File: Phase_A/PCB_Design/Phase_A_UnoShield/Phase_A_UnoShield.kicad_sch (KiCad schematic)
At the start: 23 parts, among them J1 Power, J2 Digital/PWM, J3 Analog, J4 Digital/PWM, SW1 SW_Push, SW2 SW_Push, U1 CA56-12EWA, U2 74HC595

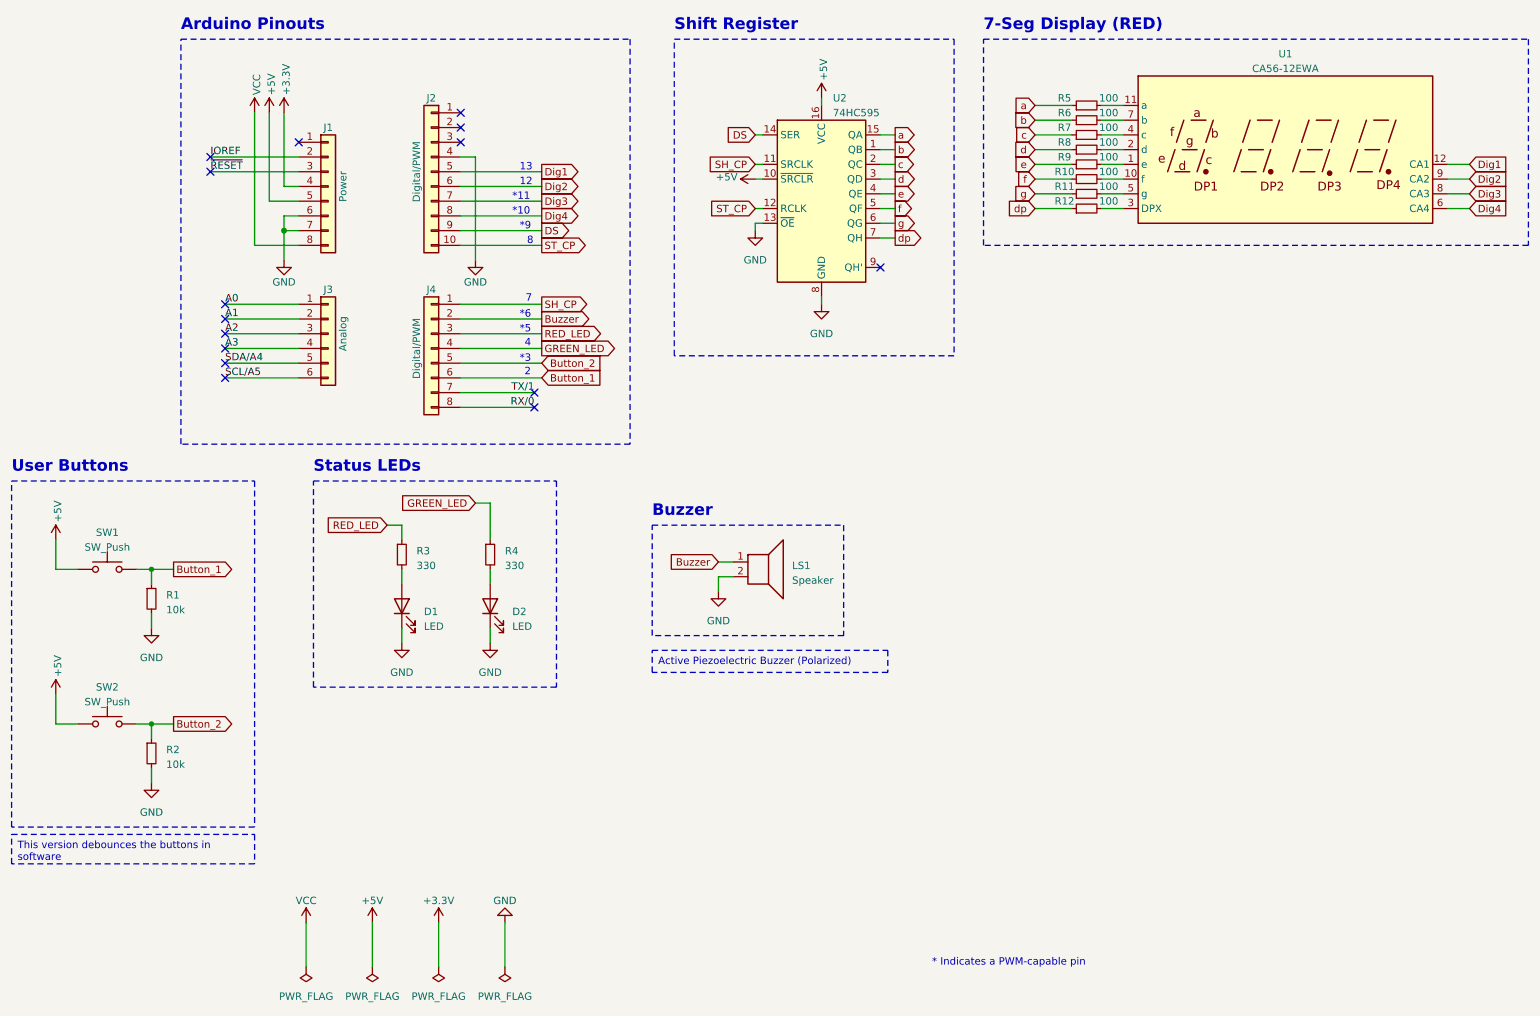
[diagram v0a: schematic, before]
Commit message: Folder Structure Update
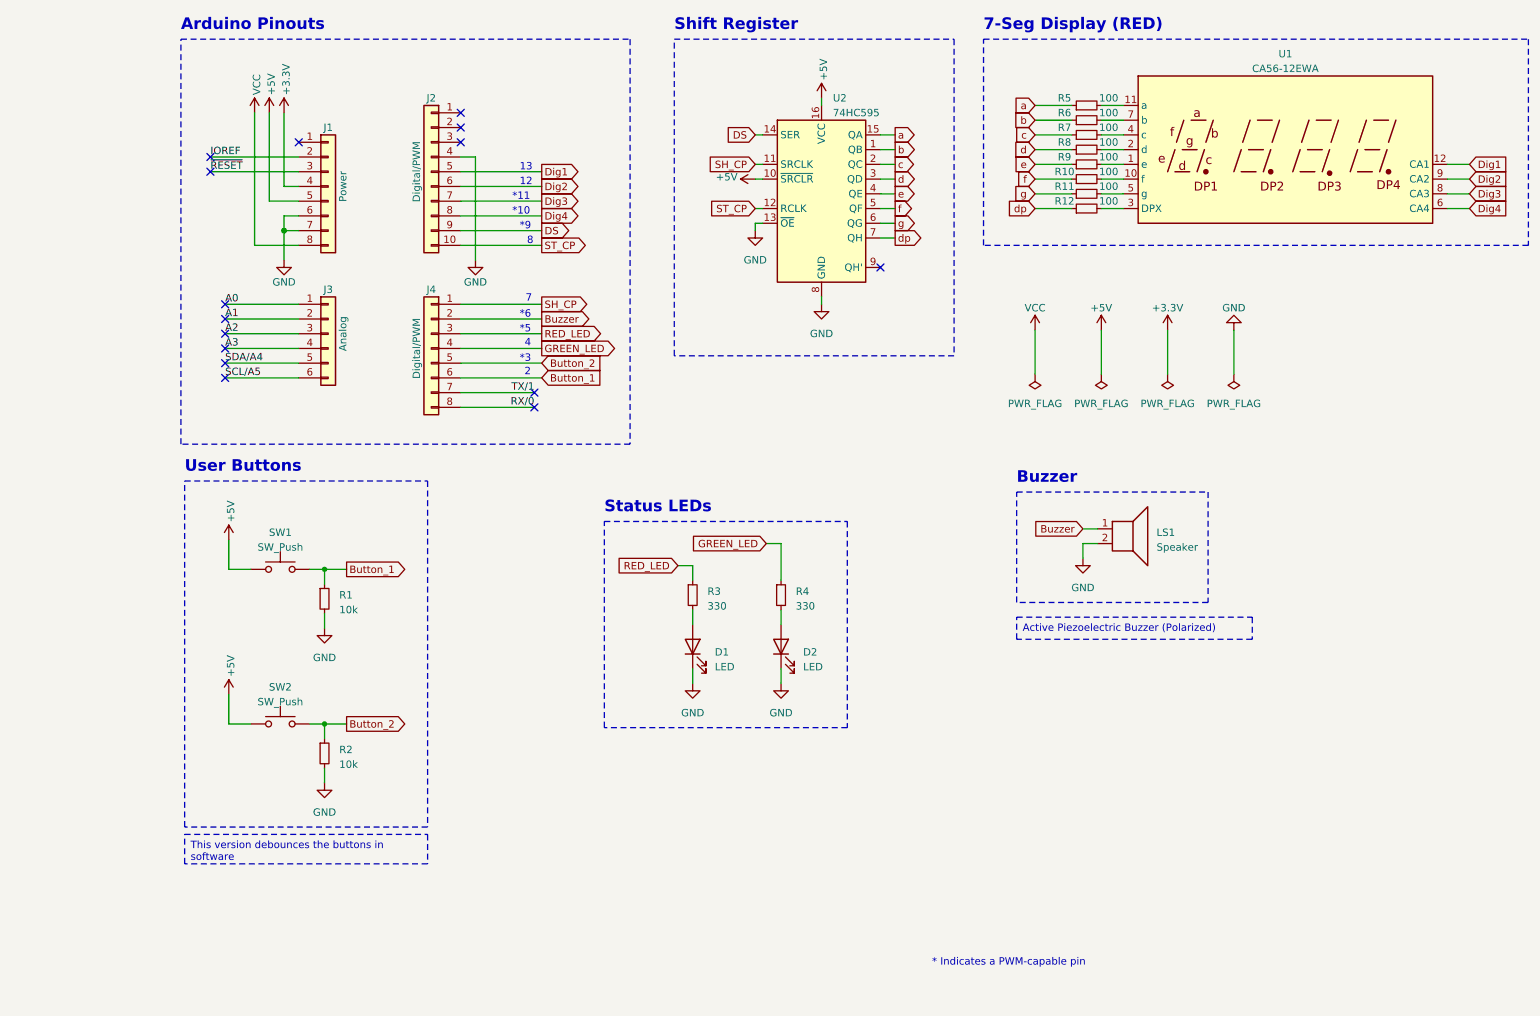
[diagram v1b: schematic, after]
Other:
- moved on the sheet: D1, D2, LS1, R1, R2, R3, R4, SW1, SW2
